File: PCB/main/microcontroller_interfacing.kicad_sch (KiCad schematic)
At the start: 21 parts, among them IC3 AT24C256C-SSHL-T, U4 CH340G, Y1 YSX321SL

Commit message: v1.0 BOM, Gerbers & Final Designs
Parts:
- removed TP12, TP13, TP9: TestPoint, TestPoint:TestPoint_Pad_D2.0mm, symbol Connector:TestPoint
- added IC4: TXS0108EPWR, 3088_uC:SOP65P640X120-20N, symbol TXS0108EPWR:TXS0108EPWR
- added J10, J11, J12, J13: Conn_01x02_Male, conn_Molex_01_02_vert:53398-0271, symbol Connector:Conn_01x02_Male
- C11: renamed from C9; JLC Part Number (none) -> C1622; LCSC (none) -> C1622; Price (none) -> 0.004
- C12: renamed from C11; JLC Part Number (none) -> C1525; LCSC (none) -> C1525; Price (none) -> 0.0011
- C13: renamed from C10; JLC Part Number (none) -> C1525; LCSC (none) -> C1525; Price (none) -> 0.0011
- C14: renamed from C12; JLC Part Number (none) -> C1653; LCSC (none) -> C1653; Price (none) -> 0.0123
- C15: renamed from C13; JLC Part Number (none) -> C1653; LCSC (none) -> C1653; Price (none) -> 0.0123
- D7: renamed from D6; JLC Part Number (none) -> C2286; LCSC (none) -> C2286; Price (none) -> 0.0032
- D8: renamed from D7; JLC Part Number (none) -> C2286; LCSC (none) -> C2286; Price (none) -> 0.0032
- D9: renamed from D8; JLC Part Number (none) -> C2286; LCSC (none) -> C2286; Price (none) -> 0.0032
- IC3: JLC Part Number (none) -> C6482; LCSC (none) -> C6482; Price (none) -> 1.5556
- R19: renamed from R18; JLC Part Number (none) -> C17673; LCSC (none) -> C17673; Price (none) -> 0.0027
- R20: renamed from R19; JLC Part Number (none) -> C17673; LCSC (none) -> C17673; Price (none) -> 0.0027
- R21: renamed from R20; JLC Part Number (none) -> C25867; LCSC (none) -> C25867; Price (none) -> 0.0009
- R22: renamed from R21; JLC Part Number (none) -> C25867; LCSC (none) -> C25867; Price (none) -> 0.0009
- R23: renamed from R22; JLC Part Number (none) -> C25867; LCSC (none) -> C25867; Price (none) -> 0.0009
- U4: JLC Part Number (none) -> C14267; LCSC (none) -> C14267; Price (none) -> 0.5838
- Y1: JLC Part Number (none) -> C9002; LCSC (none) -> C9002; Price (none) -> 0.1054
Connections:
- net 3V3: now also IC4.2 (VCCA)
- net PA10: now also J13.2 (Pin_2); no longer U4.2 (TXD)
- net PA9: now also J12.2 (Pin_2); no longer D9.1 (K), R23.2, U4.3 (RXD)
- net PB6: now also J10.2 (Pin_2); no longer IC3.6 (SCL), TP10.1
- net PB7: now also J11.2 (Pin_2); no longer IC3.5 (SDA), TP11.1
- net USB (D+): now also IC4.18 (B2); no longer U4.5 (UD+)
- net USB (D-): now also IC4.17 (B3); no longer U4.6 (UD-)
- new net: D9.1 (K), R23.2
- new net: J13.1 (Pin_1), U4.2 (TXD)
- new net: J12.1 (Pin_1), U4.3 (RXD)
- new net: IC4.3 (A2), TP10.1, U4.5 (UD+)
- new net: IC4.4 (A3), TP11.1, U4.6 (UD-)
- new net: IC3.5 (SDA), J11.1 (Pin_1)
- new net: IC3.6 (SCL), J10.1 (Pin_1)
- new net USB(+5): IC4.19 (VCCB)
- no-connect marks 7 -> 21
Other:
- note added: "EEPROM"
- note added: "Sensing Connections"
- note added: "USB TO UART"
- note added: "v0.1: -Changed EEPROM to AT24C256C-SSHL-T -Changed Power Connections for CH340G -Added LEDs in order to see if power is flowing in traces. v0.2 - Changed the wiring of certain microcontroller pins after testing the configurations on CubeIDE. - Added test points to the data lines. - Added Not Connected flags to pins that are not connected. v0.3 - Reduced resistance of R20 and R21 so that D7 and D8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"
- note removed: "v0.1: -Changed EEPROM to AT24C256C-SSHL-T -Changed Power Connections for CH340G -Added LEDs in order to see if power is flowing in traces."
- moved on the sheet: C11, C12, C13, C14, C15, D7, D8, D9, IC3, R19, R20, R21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

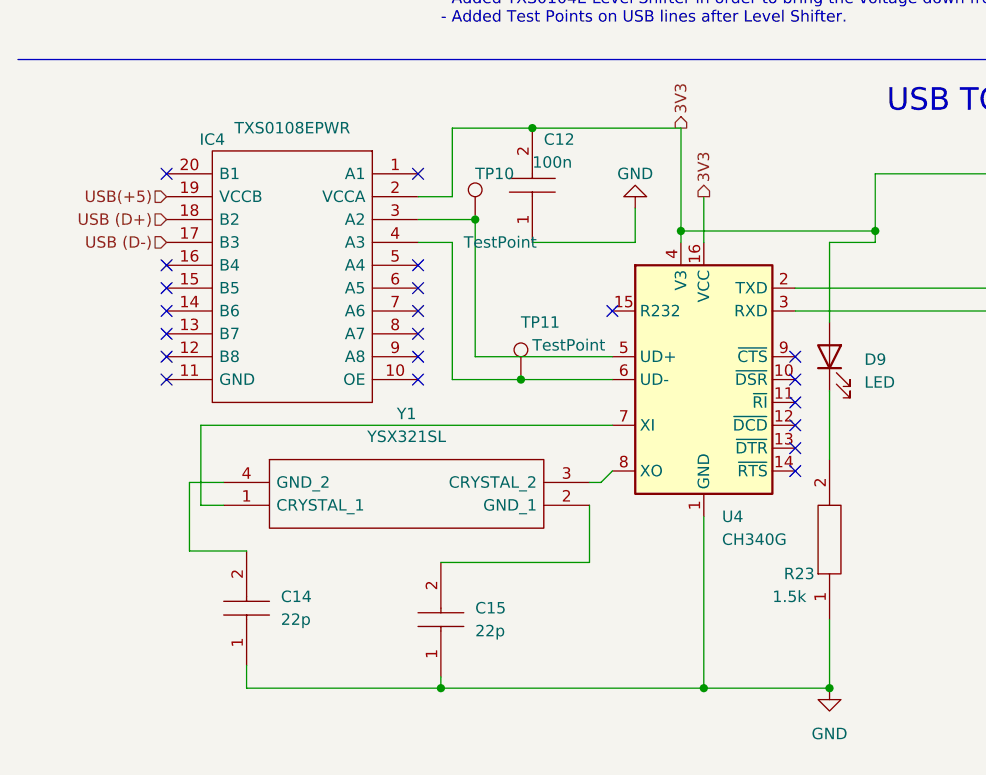
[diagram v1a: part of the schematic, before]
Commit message: Updates to Microcontroller Circuit
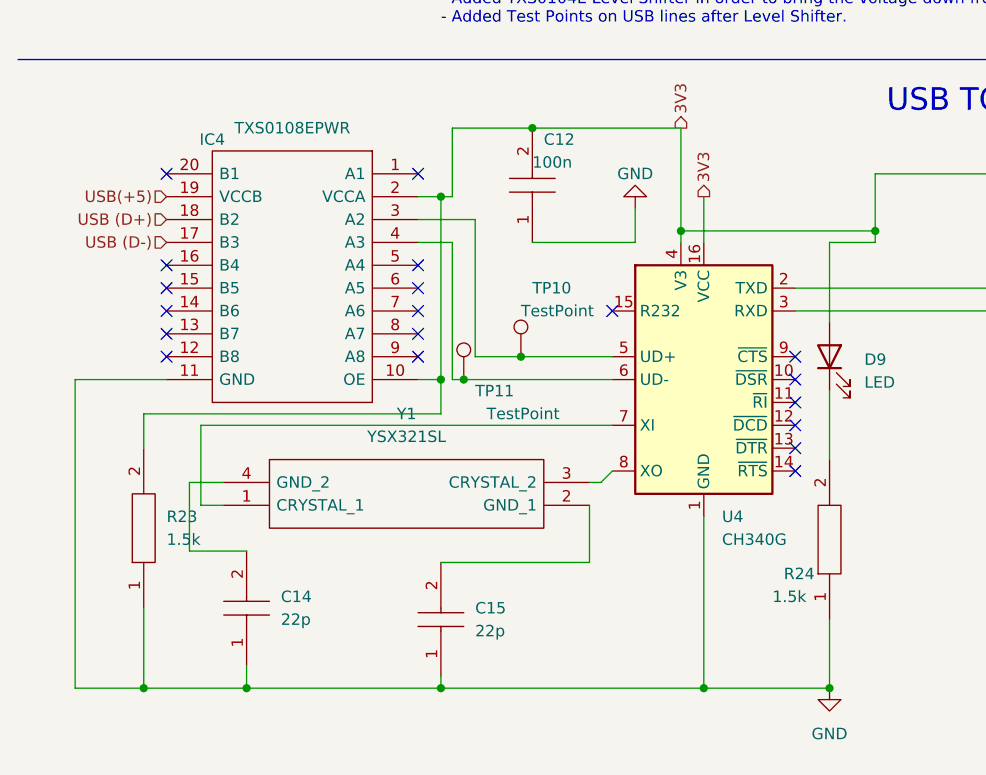
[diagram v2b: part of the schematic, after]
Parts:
- added R23: 1.5k, 4k7:RESC2013X65N, symbol 0402WGF4701TCE:0402WGF4701TCE
- R19, R20: JLC Part Number C17673 -> (none); LCSC C17673 -> (none); Price 0.0027 -> (none)
- renumbered R23 to R24
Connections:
- net 3V3: now also IC4.10 (OE), R23.2
- net GND: now also IC4.11 (GND), R23.1
- no-connect marks 21 -> 19
